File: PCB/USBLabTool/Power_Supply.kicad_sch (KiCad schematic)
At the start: 30 parts, among them U10 r1283, U7 Opamp_Quad, U8 Opamp_Quad, U9 DG403

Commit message: Starting PCB layout
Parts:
- removed C35, C36, C37: 100n, Capacitor_SMD:C_0603_1608Metric_Pad1.08x0.95mm_HandSolder, symbol Device:C
- removed D5: LM4040-5, Package_TO_SOT_SMD:SOT-23, symbol Device:D_Zener
- removed R47: 1K, Resistor_SMD:R_0603_1608Metric, symbol Device:R
- removed TP5: TestPoint, TestPoint:TestPoint_THTPad_1.5x1.5mm_Drill0.7mm, symbol Connector:TestPoint
- removed U8: Opamp_Quad, awg_fp_lib:SOIC-14, symbol Device:Opamp_Quad
- added C1, C41, C43: 10u, Capacitor_SMD:C_0603_1608Metric_Pad1.08x0.95mm_HandSolder, symbol Device:C
- added C2: 1.5u, Capacitor_SMD:C_0603_1608Metric_Pad1.08x0.95mm_HandSolder, symbol Device:C
- added C3: 1m, Capacitor_SMD:C_0603_1608Metric_Pad1.08x0.95mm_HandSolder, symbol Device:C
- added C42: 1u, Capacitor_SMD:C_0603_1608Metric_Pad1.08x0.95mm_HandSolder, symbol Device:C
- added C44, C45: 100n, Capacitor_SMD:C_0603_1608Metric_Pad1.08x0.95mm_HandSolder, symbol Device:C
- added D7: LED, LED_THT:LED_D5.0mm, symbol Device:LED
- added J2: Conn_01x01, Connector_PinHeader_2.54mm:PinHeader_1x01_P2.54mm_Vertical, symbol Connector_Generic:Conn_01x01
- added J25: T_N5V, Connector_PinHeader_2.54mm:PinHeader_1x01_P2.54mm_Vertical, symbol Connector_Generic:Conn_01x01
- added J3: T_P5V, Connector_PinHeader_2.54mm:PinHeader_1x01_P2.54mm_Vertical, symbol Connector_Generic:Conn_01x01
- added P2: USB_C_Plug_USB2.0, Connector_USB:USB_C_Receptacle_JAE_DX07S016JA1R1500, symbol Connector:USB_C_Plug_USB2.0
- added Q1: IRLML6402TRPBF, Package_TO_SOT_SMD:SOT-23-3, symbol dk_Transistors-FETs-MOSFETs-Single:IRLML6402TRPBF
- added R1: 27k, Resistor_SMD:R_0603_1608Metric_Pad0.98x0.95mm_HandSolder, symbol Device:R
- added R53: 1K, Resistor_SMD:R_0603_1608Metric, symbol Device:R
- added R62: 1K5, Resistor_SMD:R_0603_1608Metric, symbol Device:R
- added U10: Opamp_Quad, Package_SO:SOIC-14W_7.5x9mm_P1.27mm, symbol Device:Opamp_Quad
- added U11: LTC1983ES6-5#TRPBF, Package_TO_SOT_SMD:SOT-23-6_Handsoldering, symbol LTC1983ES6-5_TRPBF:LTC1983ES6-5#TRPBF
- L3: renamed from L2; footprint awg_fp_lib:NRH2410 -> footprints:IND_TAIYO_NRH2410_TAY
- L4: renamed from L3; footprint awg_fp_lib:NRH2410 -> footprints:IND_TAIYO_NRH2410_TAY
- U14: renamed from U10; footprint awg_fp_lib:DFN-12 -> Package_DFN_QFN:ST_UFDFPN-12-1EP_3x3mm_P0.5mm_EP1.4x2.55mm
- U9: renamed from U7; footprint awg_fp_lib:SOIC-14 -> Package_SO:SOIC-14W_7.5x9mm_P1.27mm; BUY (none) -> https://www.digikey.com/en/products/detail/onsemi/MC33274AD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
- renumbered C25 to C31, C26 to C32, C27 to C33, C28 to C34, C29 to C35, C30 to C36, C31 to C37, C32 to C38, C33 to C39, C34 to C40, D3 to D5, D4 to D6, R41 to R56, R42 to R57, R43 to R58, R44 to R59, R45 to R60, R46 to R61, U9 to U12
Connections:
- net +12V: now also C44.1, D7.2 (A), U10.4 (V+)
- net +3.3V: now also R62.2
- net +5V: now also C2.2, C3.1, C41.1, J3.1 (Pin_1), Q1.3 (D), U11.1 (VIN), U11.6 (~{SHDN})
- net -12V: now also C45.2, U10.11 (V-)
- net -5V: now also C43.1, J25.1 (Pin_1), U11.2 (VOUT)
- net GND: now also C1.2, C3.2, C41.2, C43.2, C44.2, C45.1, P2.A1 (GND), P2.A12 (GND), P2.B1 (GND), P2.B12 (GND), Q1.1 (G), R1.2, R53.2, U11.5 (GND)
- new net: C42.1, U11.3 (C+)
- new net: C42.2, U11.4 (C-)
- new net: D7.1 (K), R53.1
- new net: C1.1, J2.1 (Pin_1), P2.A4 (VBUS), P2.A9 (VBUS), P2.B4 (VBUS), P2.B9 (VBUS), Q1.2 (S)
- new net: C2.1, R1.1
- new net USB_DM: P2.A7 (D-)
- new net USB_DP: P2.A6 (D+), R62.1
- no-connect marks 0 -> 3
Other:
- note added: "Edit1:move these things to the Power_Supply sheet -5V might not be needed (awg already has it?) usb plug should be with MCU probably (psu part on power supply)"
- note added: "Edit2: Already moved to PSU. Keep the -5V as backup"
- note added: "Negative 5V Power supply"
- note added: "USB Soft Start Schematic"
- note added: "Vout"
- note removed: "-5V reference"

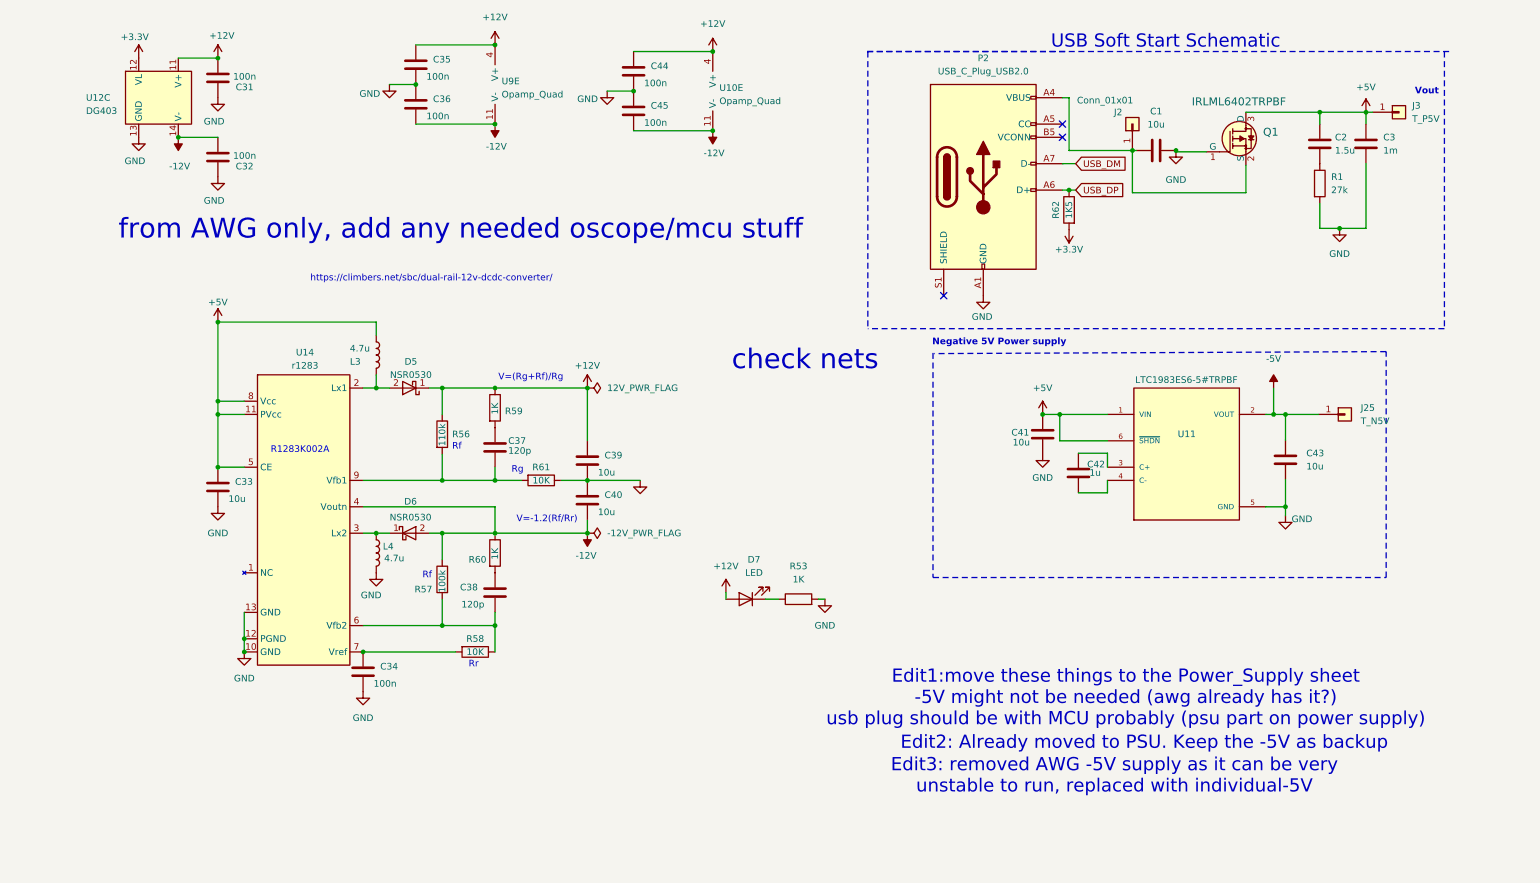
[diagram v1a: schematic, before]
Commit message: Moving files to where they should be
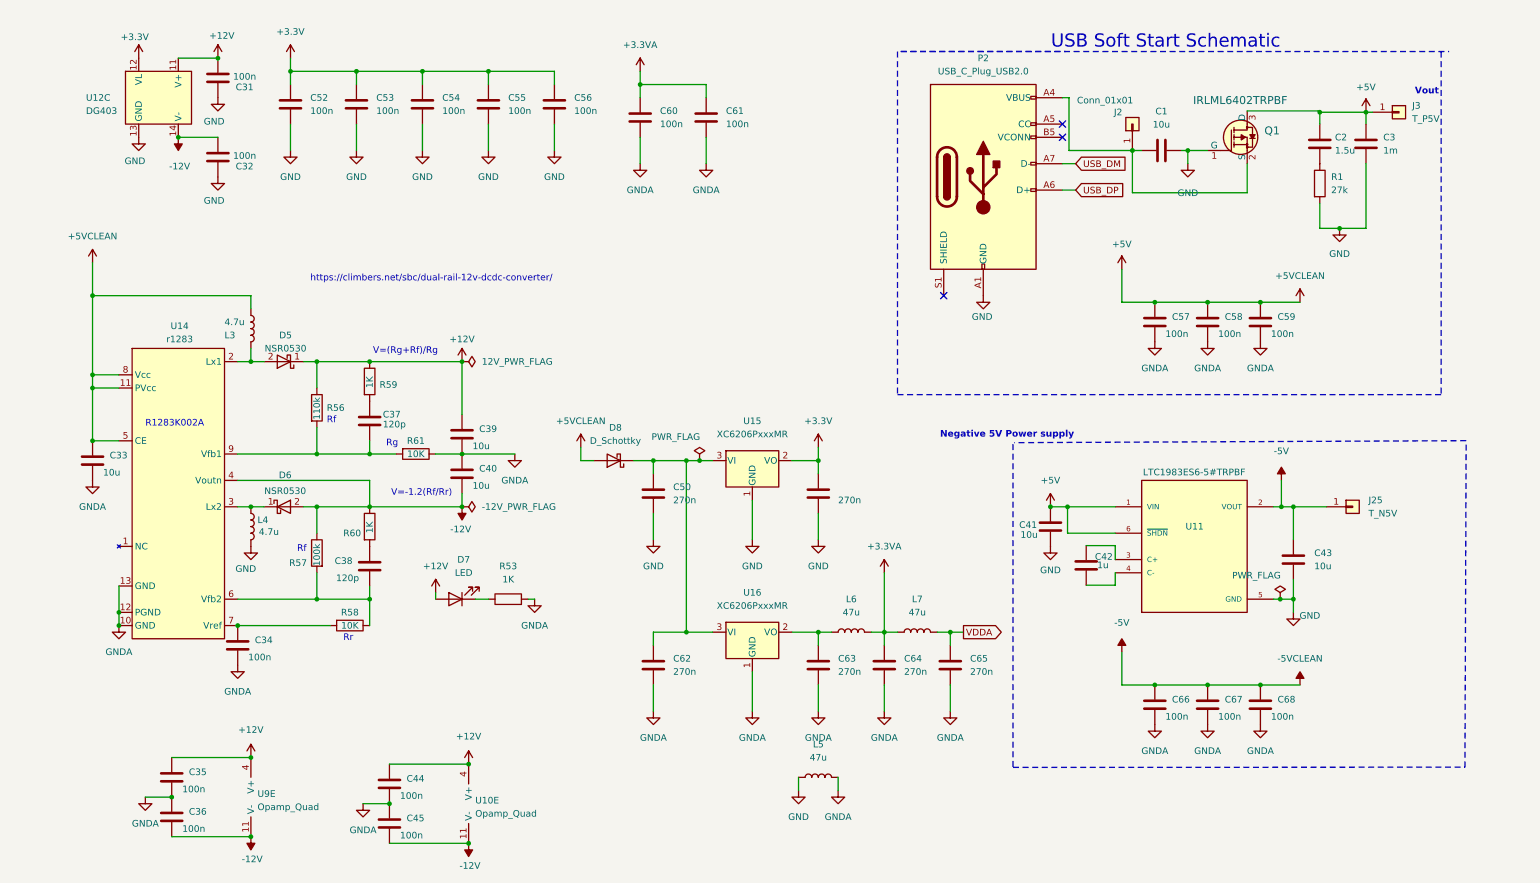
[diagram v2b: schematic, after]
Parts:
- removed R62: 1K5, Resistor_SMD:R_0603_1608Metric, symbol Device:R
- added C50, C51, C62, C63, C64, C65: 270n, Capacitor_SMD:C_0603_1608Metric_Pad1.08x0.95mm_HandSolder, symbol Device:C
- added C52, C53, C54, C55, C56, C57, C58, C59, C60, C61, C66, C67, C68: 100n, Capacitor_SMD:C_0603_1608Metric_Pad1.08x0.95mm_HandSolder, symbol Device:C
- added D8: D_Schottky, Diode_SMD:D_1206_3216Metric_Pad1.42x1.75mm_HandSolder, symbol Device:D_Schottky
- added L5, L6, L7: 47u, Inductor_SMD:L_0603_1608Metric_Pad1.05x0.95mm_HandSolder, symbol Device:L
- added U15, U16: XC6206PxxxMR, Package_TO_SOT_SMD:SOT-23-3, symbol Regulator_Linear:XC6206PxxxMR
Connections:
- net +3.3V: now also C51.1, C52.1, C53.1, C54.1, C55.1, C56.1, U15.2 (VO)
- net +5V: now also C57.1, C58.1, C59.1, D8.2 (A)
- net -5V: now also C66.1, C67.1, C68.1
- net GND: now also C50.2, C51.2, C52.2, C53.2, C54.2, C55.2, C56.2, L5.1, U15.1 (GND); no longer C33.2, C34.2, C35.2, C36.1, C39.2, C40.1, C44.2, C45.1, R53.2, R61.1, U14.10 (GND), U14.12 (PGND), U14.13 (GND)
- new net: C63.1, L6.1, U16.2 (VO)
- new net: C50.1, C62.1, D8.1 (K), U15.3 (VI), U16.3 (VI)
- new net +3.3VA: C60.1, C61.1, C64.1, L6.2, L7.1
- new net GNDA: C33.2, C34.2, C35.2, C36.1, C39.2, C40.1, C44.2, C45.1, C57.2, C58.2, C59.2, C60.2, C61.2, C62.2, C63.2, C64.2, C65.2, C66.2, C67.2, C68.2, L5.2, R53.2, R61.1, U14.10 (GND), U14.12 (PGND), U14.13 (GND), U16.1 (GND)
- new net VDDA: C65.1, L7.2
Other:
- note removed: "Edit1:move these things to the Power_Supply sheet -5V might not be needed (awg already has it?) usb plug should be with MCU probably (psu part on power supply)"
- note removed: "Edit2: Already moved to PSU. Keep the -5V as backup"
- note removed: "check nets"
- note removed: "from AWG only, add any needed oscope/mcu stuff"
- moved on the sheet: C1, C33, C34, C35, C36, C37, C38, C39, C40, C41, C42, C43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

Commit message: Moving files to where they should be
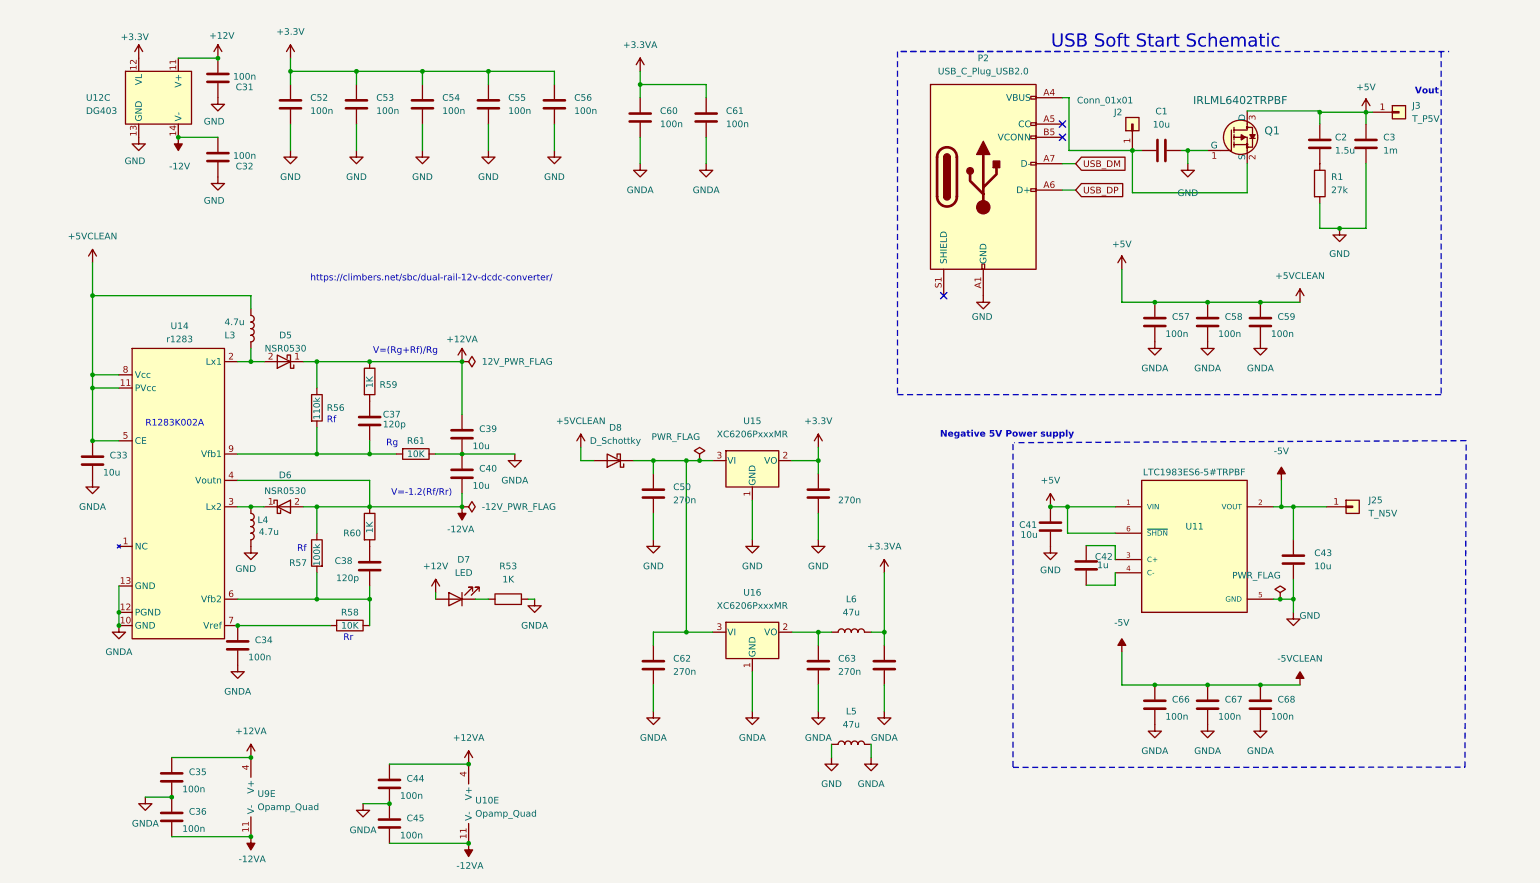
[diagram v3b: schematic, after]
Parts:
- removed C65: 270n, Capacitor_SMD:C_0603_1608Metric_Pad1.08x0.95mm_HandSolder, symbol Device:C
- removed L7: 47u, Inductor_SMD:L_0603_1608Metric_Pad1.05x0.95mm_HandSolder, symbol Device:L
- C3: footprint Capacitor_SMD:C_0603_1608Metric_Pad1.08x0.95mm_HandSolder -> Capacitor_THT:CP_Radial_D10.0mm_P5.00mm
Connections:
- net +12V: no longer C35.1, C39.1, C44.1, D5.1 (K), R56.1, R59.1, U10.4 (V+), U9.4 (V+)
- net -12V: no longer C36.2, C40.2, C45.2, D6.2 (A), R57.1, R60.1, U10.11 (V-), U14.4 (Voutn), U9.11 (V-)
- new net +12VA: C35.1, C39.1, C44.1, D5.1 (K), R56.1, R59.1, U10.4 (V+), U9.4 (V+)
- new net -12VA: C36.2, C40.2, C45.2, D6.2 (A), R57.1, R60.1, U10.11 (V-), U14.4 (Voutn), U9.11 (V-)
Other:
- moved on the sheet: L5

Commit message: Routed revised PCB
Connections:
- net +12V is gone; now on net +12VA: C31.2, D7.2 (A), U12.11 (V+)
- net -12V is gone; now on net -12VA: C32.2, U12.14 (V-)
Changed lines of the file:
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@@
 				)
 				(justify left)
-				(hide yes)
 			)
 		)
@@
 			)
 		)
-		(property "Value" "-12V"
+		(property "Value" "-12VA"
 			(at 35.814 44.958 0)
 			(effects
@@
 			)
 		)
-		(property "Value" "+12V"
+		(property "Value" "+12VA"
 			(at 43.942 19.812 0)
 			(effects
@@
 		(on_board yes)
 		(dnp no)
-		(fields_autoplaced yes)
 		(property "Reference" "#PWR071"
 			(at 85.09 130.81 0)
@@
 			)
 		)
-		(property "Value" "+12V"
-			(at 85.09 121.92 0)
+		(property "Value" "+12VA"
+			(at 79.502 122.936 0)
 			(effects
 				(font
 					(size 1.27 1.27)
 				)
+				(justify left)
 			)
 		)
